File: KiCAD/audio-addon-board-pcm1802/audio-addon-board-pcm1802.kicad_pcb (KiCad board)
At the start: 4 copper layers, 85 x 70 mm, 69 parts, among them J1 RCA, J2 CONN_HOST_1, J3 RCA, J4 RCA, J5 RCA, SW1 SW_DIP_x04, U1 PCM1802DBR, U2 LTC1682IS8-5, U3 SN74LVC1G125DBV

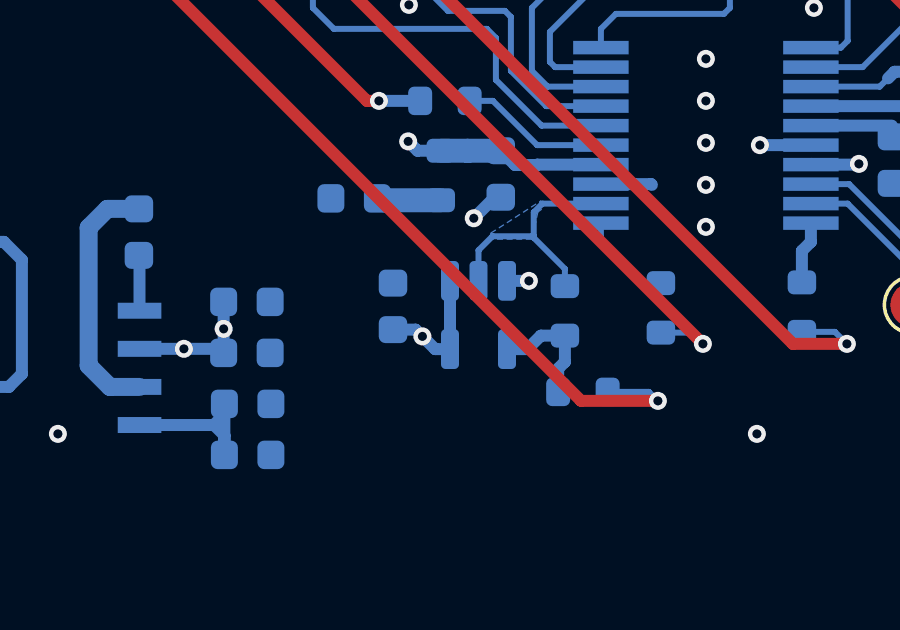
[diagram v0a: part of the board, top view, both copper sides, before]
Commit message: update schematic
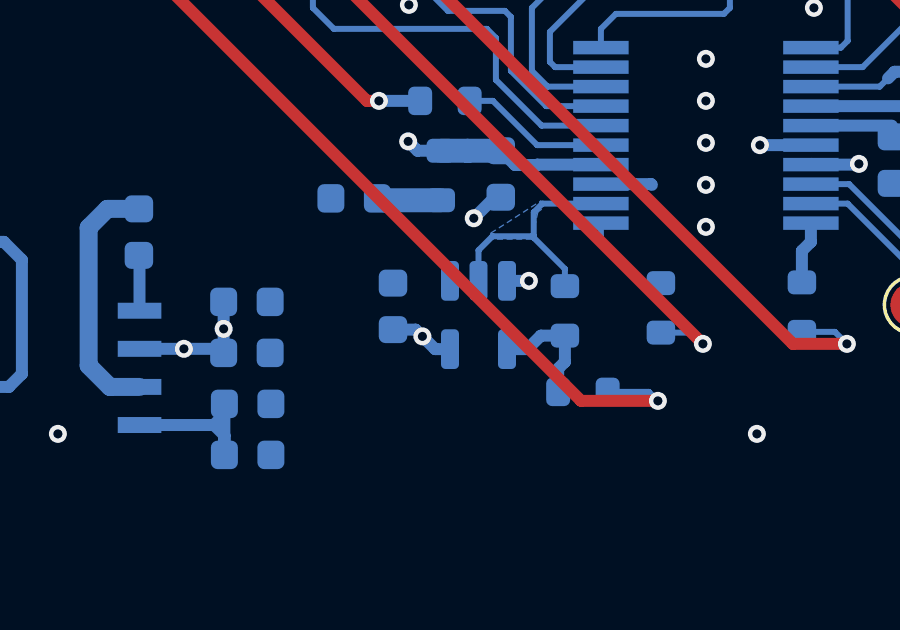
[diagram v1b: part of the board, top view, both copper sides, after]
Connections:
- U3 pad 1: +3.3V -> GND
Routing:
- net +3.3V: track 88.0 -> 85.7 mm

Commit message: initial board fixes
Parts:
- moved J2 30.6 mm to (109.3, 61.0), turned to -90 degrees
- moved J4 9.50 mm to (177.3, 110.9)
- moved J5 9.50 mm to (159.2, 110.9)
- moved J1 2.50 mm to (159.2, 55.1)
- moved J3 2.50 mm to (177.2, 55.1)
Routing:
- net Net-(J2-Pin_1): track 65.1 -> 7.85 mm
- net DOUT: track 31.1 -> 4.36 mm
- net LRCK: track 27.0 -> 1.67 mm
- net BCK: track 24.9 -> 1.56 mm
- net Net-(J2-Pin_4): track 53.5 -> 38.0 mm
- net SCKI: track 16.6 -> 1.78 mm
- net Net-(J1-In): track 26.8 -> 29.3 mm
- net Net-(J3-In): track 15.2 -> 17.7 mm
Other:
- board size 85 x 70 mm -> 85 x 82 mm

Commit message: initial board fixes
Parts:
- removed R8, RBYPASS2, RFMT2, RFMT4, RMODE2, RMODE4, ROSR2: 0R, Resistor_SMD:R_0603_1608Metric
- removed RBYPASS1, RFMT0, RFMT1, RMODE0, RMODE1, ROSR1: NP, Resistor_SMD:R_0603_1608Metric
- removed TP1: TestPoint, TestPoint:TestPoint_Pad_D1.5mm
- added H1: MountingHole, MountingHole:MountingHole_3.2mm_M3_DIN965_Pad_TopBottom, F.Cu at (103.4, 59.7)
- added H2: MountingHole, MountingHole:MountingHole_3.2mm_M3_DIN965_Pad_TopBottom, F.Cu at (145.7, 59.7)
- added H3: MountingHole, MountingHole:MountingHole_3.2mm_M3_DIN965_Pad_TopBottom, F.Cu at (103.4, 125.2)
- added H4: MountingHole, MountingHole:MountingHole_3.2mm_M3_DIN965_Pad_TopBottom, F.Cu at (145.7, 125.2)
- added JBYPASS1: Jumper, Jumper:SolderJumper-3_P1.3mm_Bridged12_RoundedPad1.0x1.5mm, B.Cu at (142.3, 77.2)
- added JFMT0: Jumper, Jumper:SolderJumper-3_P1.3mm_Bridged12_RoundedPad1.0x1.5mm, B.Cu at (117.6, 64.4)
- added JFMT1: Jumper, Jumper:SolderJumper-3_P1.3mm_Bridged12_RoundedPad1.0x1.5mm, B.Cu at (122.6, 64.4)
- added JMODE0: Jumper, Jumper:SolderJumper-3_P1.3mm_Bridged12_RoundedPad1.0x1.5mm, B.Cu at (132.8, 64.4)
- added JMODE1: Jumper, Jumper:SolderJumper-3_P1.3mm_Bridged12_RoundedPad1.0x1.5mm, B.Cu at (127.7, 64.4)
- added JOSR1: Jumper, Jumper:SolderJumper-3_P1.3mm_Bridged12_RoundedPad1.0x1.5mm, B.Cu at (112.4, 64.4)
- added JP1: Jumper_2_Small_Bridged, Jumper:SolderJumper-2_P1.3mm_Bridged_RoundedPad1.0x1.5mm, B.Cu at (147.8, 78.0)
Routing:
- net Net-(J2-Pin_1): track 7.85 -> 97.6 mm
- net LRCK: track 1.67 -> 48.3 mm
- net Net-(J2-Pin_4): track 38.0 -> 80.3 mm
- net BCK: track 1.56 -> 34.5 mm
- net /+3v3 from host: track 15.1 -> 41.8 mm, vias 0 -> 1
- net DOUT: track 4.36 -> 28.4 mm
- net SCKI: track 1.78 -> 18.5 mm
- net GND: track 53.9 -> 67.5 mm, vias 19 -> 20
- net Net-(J4-In): track 45.8 -> 55.4 mm
- net Net-(J5-In): track 30.4 -> 39.9 mm
- net +3.3V: track 85.7 -> 94.6 mm
- net Net-(JOSR1-C): track 14.8 -> 19.8 mm
- net Net-(JFMT0-C): track 10.6 -> 14.2 mm
- net Net-(JMODE1-C): track 7.28 -> 5.38 mm
- net Net-(JMODE0-C): track 8.02 -> 6.18 mm
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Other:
- outline, holes or cut-outs redrawn

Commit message: initial board fixes
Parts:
- moved H3 2.90 mm to (103.3, 128.1)
- moved H4 2.90 mm to (145.6, 128.1)
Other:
- outline, holes or cut-outs redrawn
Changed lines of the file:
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@@
 	(footprint "MountingHole:MountingHole_3.2mm_M3_DIN965_Pad_TopBottom"
 		(layer "F.Cu")
-		(at 103.4 125.2)
+		(at 103.3 128.1)
 		(descr "Mounting Hole 3.2mm, M3, generated by kicad-footprint-generator mountinghole.py")
 		(tags "mountinghole M3 DIN965")
@@
 	(footprint "MountingHole:MountingHole_3.2mm_M3_DIN965_Pad_TopBottom"
 		(layer "F.Cu")
-		(at 145.7 125.2)
+		(at 145.6 128.1)
 		(descr "Mounting Hole 3.2mm, M3, generated by kicad-footprint-generator mountinghole.py")
 		(tags "mountinghole M3 DIN965")
@@
 		(stroke
 			(width 0.05)
+			(type default)
+		)
+		(layer "Edge.Cuts")
+	)
+	(gr_line
+		(start 103.4 59.7)
+		(end 103.3 128.1)
+		(stroke
+			(width 0.05)

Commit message: board fixes, finished
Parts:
- removed C25: 1uF, Capacitor_SMD:C_0603_1608Metric
- removed R1, R2, R22: 1R, Resistor_SMD:R_0603_1608Metric
- removed R12: NP, Resistor_SMD:R_0603_1608Metric
- removed R3: 0R, Resistor_SMD:R_0603_1608Metric
- removed U3: SN74LVC1G125DBV, Package_TO_SOT_SMD:SOT-23-5
- moved R11 75.4 mm to (109.0, 54.8)
- moved C23 75.2 mm to (109.0, 53.2)
- moved R14 71.4 mm to (112.3, 53.2), turned to 0 degrees
- moved R9 66.9 mm to (112.3, 54.8)
- moved C24 63.1 mm to (115.5, 54.8), turned to 180 degrees
- moved R13 62.9 mm to (115.5, 53.2), turned to 180 degrees
- moved C12 31.8 mm to (181.5, 89.2), turned to 90 degrees
- moved RA3 31.4 mm to (181.5, 84.5), turned to 90 degrees
- moved C18 29.3 mm to (178.2, 76.9), turned to 180 degrees
- moved RA1 28.4 mm to (178.2, 78.6), turned to 180 degrees
- moved C20 27.3 mm to (177.5, 92.1), turned to -90 degrees
- moved C19 25.3 mm to (175.0, 76.9), turned to 180 degrees
- moved C21 25.1 mm to (175.8, 92.1), turned to -90 degrees
- moved SW1 24.5 mm to (176.6, 84.6), turned to 90 degrees
- moved RA2 24.3 mm to (175.1, 78.6), turned to 0 degrees
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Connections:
- C15 pad 2: Net-(C15-Pad2) -> +3.3V
- C9 pad 1: Net-(C9-Pad1) -> Net-(U1-VREF1)
- CNP1 pad 1: Net-(CNP1-Pad1) -> Net-(U1-VREF2)
- H1 pad 1: GND -> (no net)
- R10 pad 1: Net-(R10-Pad1) -> Net-(U1-DOUT)
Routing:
- net Net-(J2-Pin_1): track 97.6 -> 13.6 mm
- net Net-(J2-Pin_4): track 80.3 -> 7.44 mm, vias 1 -> 0
- net Net-(J3-In): track 17.7 -> 85.7 mm, vias 0 -> 1
- net VINL: track 25.0 -> 56.7 mm, vias 0 -> 2
- net Net-(J4-In): track 55.4 -> 25.3 mm, vias 0 -> 1
- net VINR: track 23.1 -> 51.7 mm, vias 0 -> 2
- net +3.3V: track 94.6 -> 70.1 mm, vias 15 -> 13
- net Net-(J1-In): track 29.3 -> 52.3 mm, vias 0 -> 2
- net Net-(J5-In): track 39.9 -> 28.7 mm, vias 0 -> 1
- net Net-(R10-Pad1): track 4.08 -> 0.00 mm
- net DOUT: track 28.4 -> 31.0 mm
- net Net-(U1-DOUT): track 8.30 -> 5.87 mm
- net Net-(C15-Pad2): track 2.04 -> 0.00 mm
- net Net-(U1-VREF2): track 10.6 -> 12.6 mm
- net Net-(CNP1-Pad1): track 1.91 -> 0.00 mm
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- removed copper zone on B.Cu, net Net-(U1-DOUT)
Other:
- board size 85 x 82 mm -> 85 x 83.9 mm
- board text added: "*"

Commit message: board fixes, finished
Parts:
- added D1: LED, LED_SMD:LED_0603_1608Metric, B.Cu at (103.4, 86.9)
- added D2: LED, LED_SMD:LED_0603_1608Metric, B.Cu at (103.4, 72.5)
- added R1: 1k, Resistor_SMD:R_0603_1608Metric, B.Cu at (103.4, 84.9)
- added R2: 1k, Resistor_SMD:R_0603_1608Metric, B.Cu at (103.4, 70.6)
- renumbered JP1 to JFSYNC1
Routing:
- net +3.3V: track 70.1 -> 78.7 mm
- net /+5V, Analog: track 72.6 -> 78.0 mm
- net Net-(D1-A): track 0.00 -> 2.02 mm
- net Net-(D2-A): track 0.00 -> 1.92 mm
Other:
- board text added: "3v3"
- board text added: "5V"
- board text added: "ADC128S022 (Low Quality)"

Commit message: board fixes
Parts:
- D1, D2: footprint LED_SMD:LED_0603_1608Metric -> LED_SMD:LED_0805_2012Metric
- moved R10 1.88 mm to (126.6, 76.0)
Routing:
- net LRCK: track 48.3 -> 43.4 mm
- net DOUT: track 31.0 -> 27.4 mm
- net GND: track 67.9 -> 71.4 mm
- net Net-(U1-DOUT): track 5.87 -> 3.64 mm

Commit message: update board
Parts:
- moved JFSYNC1 9.63 mm to (138.2, 77.2)
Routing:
- net Net-(JFSYNC1-B): track 15.1 -> 5.20 mm
- net +3.3V: track 78.7 -> 75.2 mm, vias 13 -> 14
- net GND: track 71.4 -> 70.3 mm
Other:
- board text added: "JLCJLCJLCJLC"
- board text removed: "JLCJLCJLC"
